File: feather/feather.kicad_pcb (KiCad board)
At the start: 4 copper layers, 61.4 x 38.8 mm, 146 parts, among them CN1 ST-0337D00-071-1A2H, CN2 GT-3321667P-01, J1 Connector, USB-TYPE-C-16P, SW1 1TS015A-1400-0600-CT, SW2 1TS015A-1400-0600-CT, U1 TLV76733DRVx, U10 OPA1622, U11 OPA1622, U2 LM27762, U3 TAD5242IRGER, U4 TLV76733DRVx, U5 OPA1612AxD, U6 RP2350A-QFN60, U7 OPA1612AxD, U8 OPA1612AxD, U9 OPA1622, X1 12MHz

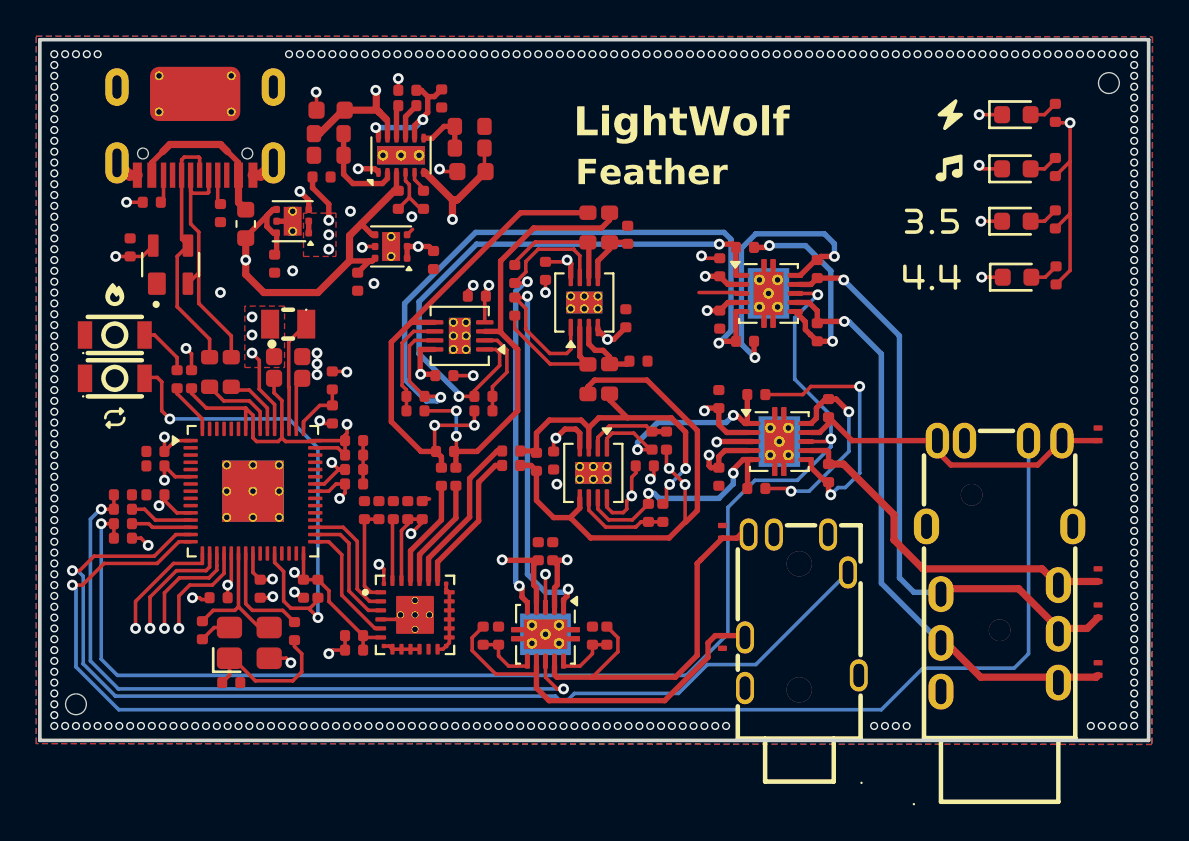
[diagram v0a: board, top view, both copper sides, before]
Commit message: feat: update power line trace width
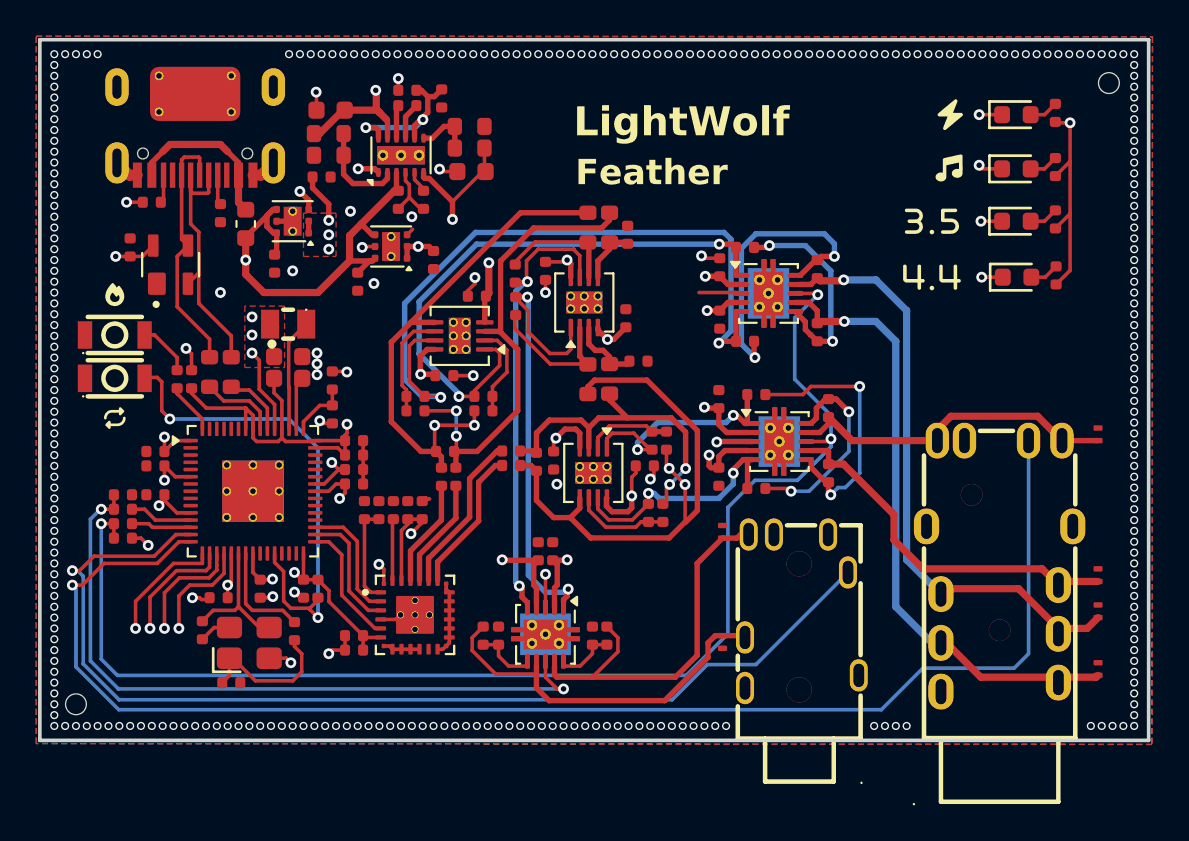
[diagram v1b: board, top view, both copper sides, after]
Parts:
- moved R18 0.06 mm to (143.8, 95.6)
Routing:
- net +4V5: track 109.7 -> 119.8 mm
- net -4V5: track 96.4 -> 98.7 mm
- net /OUT-BAL-2N: track 33.3 -> 34.9 mm
- net +AUDIO3V3: track 25.0 -> 23.8 mm
- net Net-(U2-EN+): track 7.90 -> 9.00 mm
- net /OUT-BAL-2P: track 33.0 -> 33.6 mm
- net /OUT-BAL-1P: track 18.5 -> 19.1 mm
